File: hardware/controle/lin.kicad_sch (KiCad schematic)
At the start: 19 parts, among them J8 Serial, Q1 DMG2307L, Q2 DMG2307L, Q3 BSS123, Q4 BSS123, U3 MCP2003B

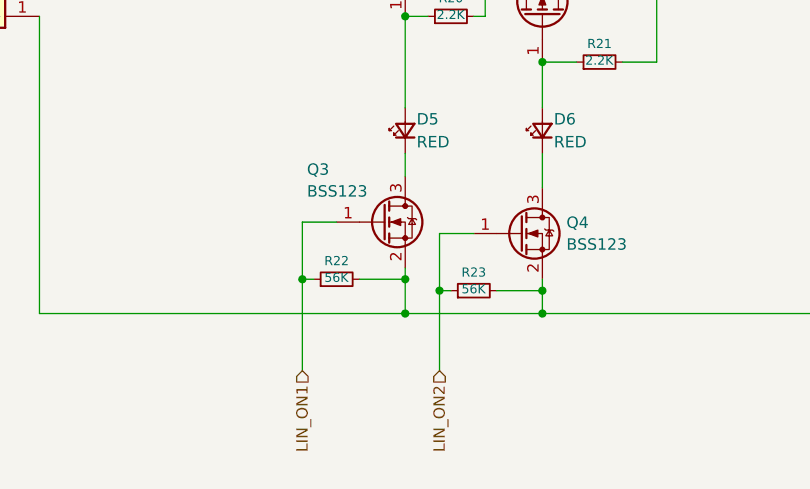
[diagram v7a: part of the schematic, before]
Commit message: rdware/controle: move back some resistors to 47k to match our stock
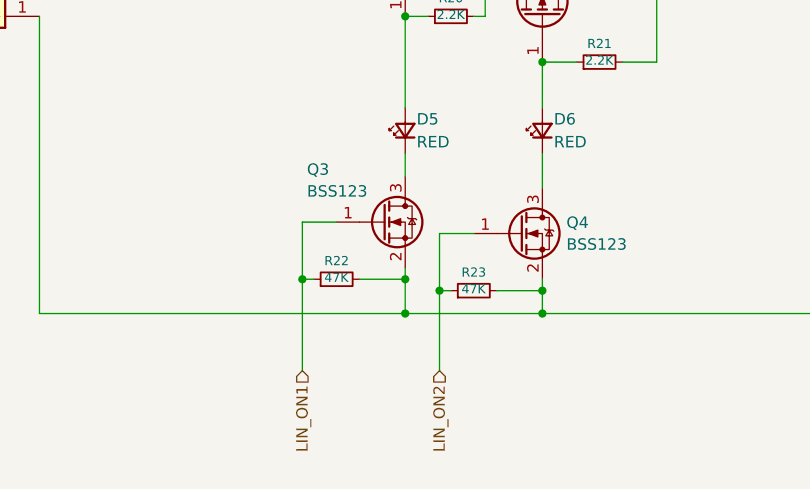
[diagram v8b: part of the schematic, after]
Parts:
- R22, R23: value 56K -> 47K; P/N MCWR08X5602FTL -> MCWR08X4702FTL
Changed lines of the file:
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@@
 			)
 		)
-		(property "Value" "56K"
+		(property "Value" "47K"
 			(at 83.7946 93.8022 90)
 			(effects
@@
 			)
 		)
-		(property "P/N" "MCWR08X5602FTL"
+		(property "P/N" "MCWR08X4702FTL"
 			(at 83.82 93.98 0)
 			(effects
@@
 			)
 		)
-		(property "Value" "56K"
+		(property "Value" "47K"
 			(at 99.0346 95.0722 90)
 			(effects
@@
 			)
 		)
-		(property "P/N" "MCWR08X5602FTL"
+		(property "P/N" "MCWR08X4702FTL"
 			(at 99.06 95.25 0)
 			(effects
